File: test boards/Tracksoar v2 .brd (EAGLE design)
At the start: 50.4 x 19.6 mm, 48 parts, among them IC1 BME280, IC2 74AHC1G125DBV, Y1 16MHZ

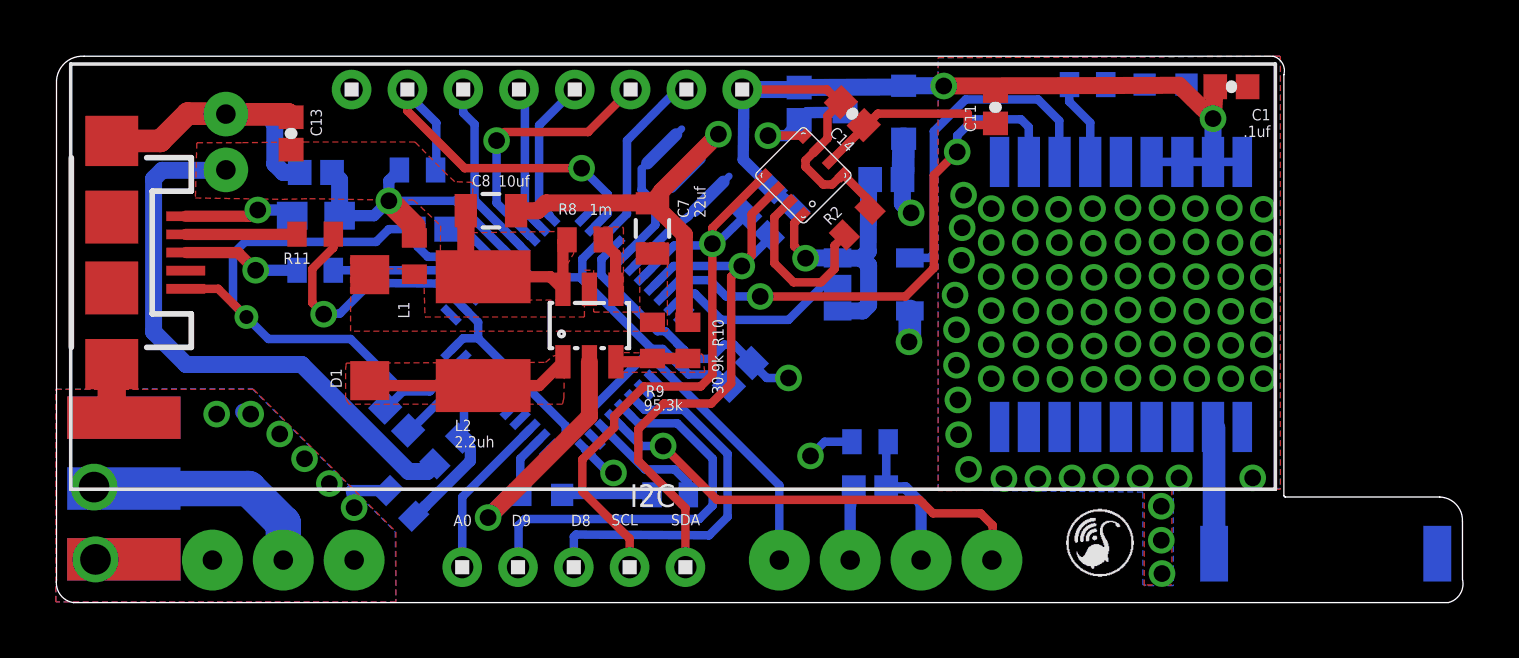
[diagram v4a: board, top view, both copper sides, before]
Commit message: Silkscreen cleanup and additional analog pin
removed as many silkscreen keep out errors as possible. Added a
breakout for analog pin A1 to the bottom header.
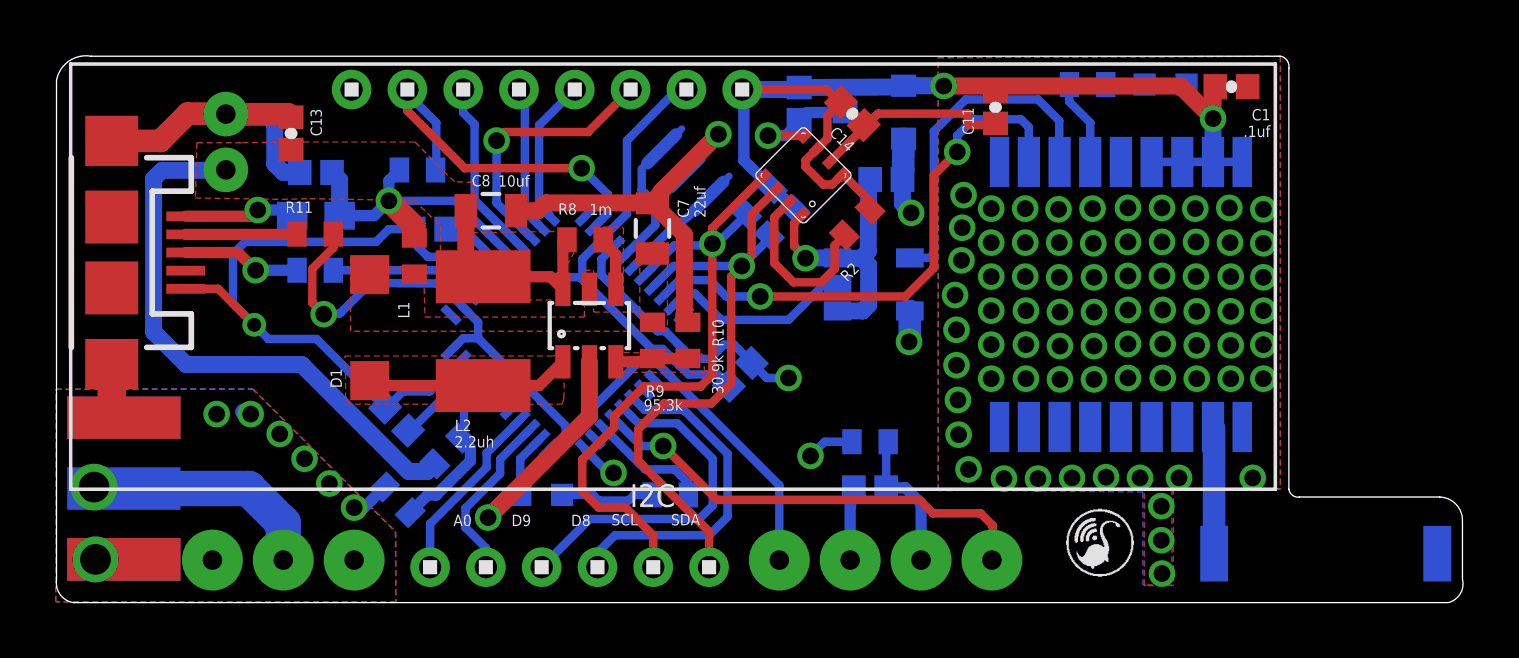
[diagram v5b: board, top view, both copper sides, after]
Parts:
- U$3: value 1X5 -> 1X6; device headers(2mm):1X5 -> headers(2mm):1X6
- moved C6 0.18 mm to (12.2, 3.66)
- moved U$3 0.15 mm to (18.4, 1.24)
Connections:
- new net A1: U$3.1, U$4.37
- net A0: now also U$3.2; no longer U$3.1
- net D8: now also U$3.4; no longer U$3.3
- net D9: now also U$3.3; no longer U$3.2
- net SCL: now also U$3.5; no longer U$3.4
- net SDA: now also U$3.6; no longer U$3.5
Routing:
- net A1: track 0.00 -> 6.63 mm
- net D9: track 14.3 -> 12.6 mm
- net D8: track 13.3 -> 12.1 mm
- net SCL: track 23.2 -> 24.1 mm
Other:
- outline, holes or cut-outs redrawn

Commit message: Moved BME280
moved the bme 280 sensor away from the 3v regulator to help mitigate thermal issues.
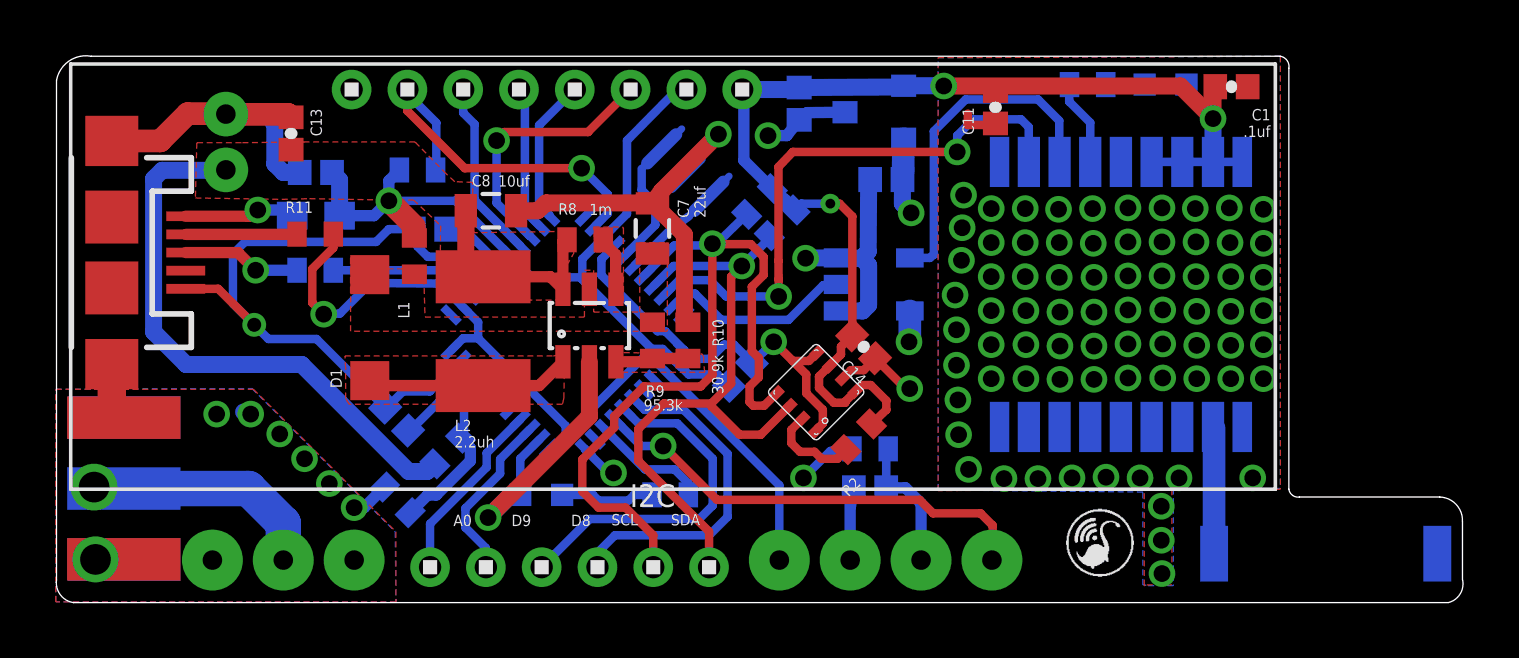
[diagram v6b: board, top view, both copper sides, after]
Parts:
- moved C14 8.37 mm to (29.0, 9.14)
- moved IC1 7.79 mm to (27.3, 7.52)
- moved R2 7.70 mm to (28.8, 5.92)
- moved R12 0.25 mm to (29.2, 5.49)
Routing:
- net SCL: track 24.1 -> 29.8 mm
- net N$2: track 6.69 -> 3.37 mm
- net 3V: track 40.5 -> 43.7 mm, vias 2 -> 3
- net RX: track 19.8 -> 20.6 mm
- net GND: track 104.0 -> 104.6 mm, vias 86 -> 87
- net SDA: track 22.6 -> 23.1 mm

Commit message: Removed Pours
removed pours from under the lm3480 to limit heat reaching the bme280
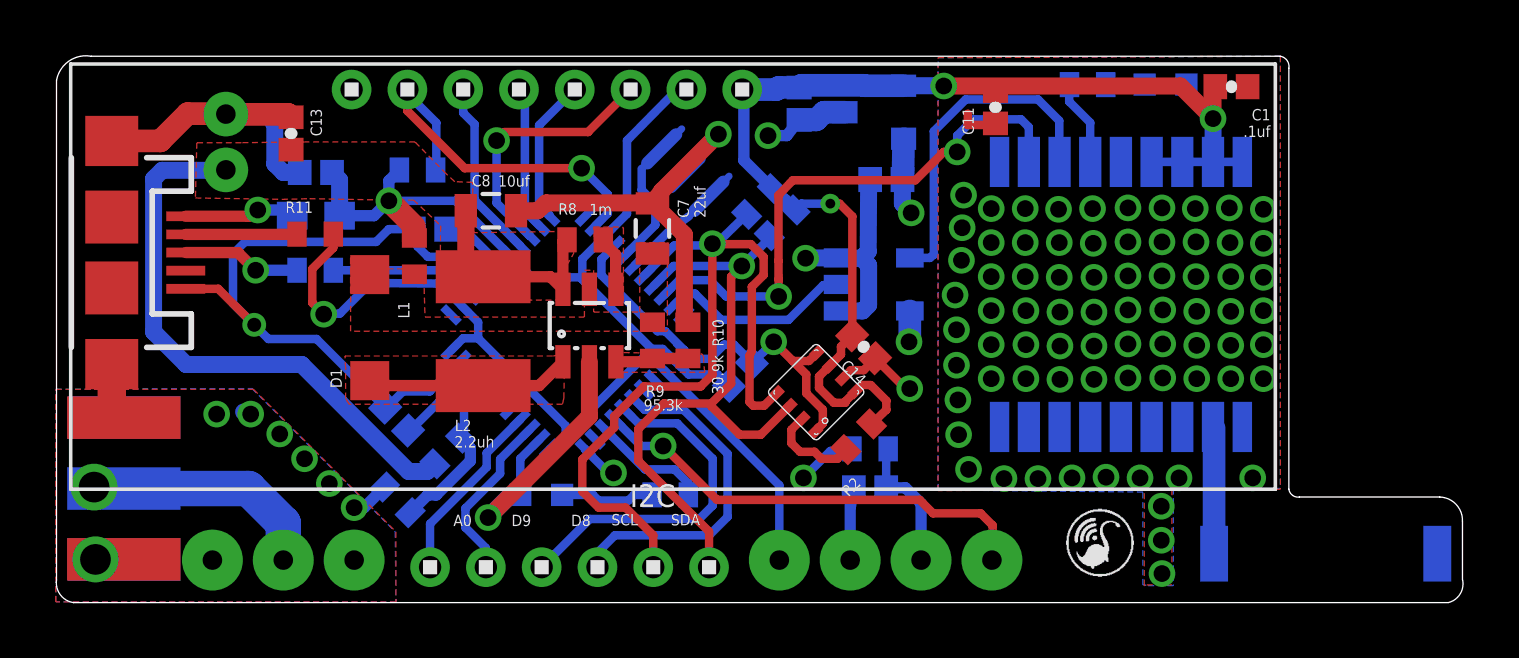
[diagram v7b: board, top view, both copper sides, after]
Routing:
- net GND: track 104.6 -> 101.8 mm
- net RX: track 20.6 -> 20.0 mm
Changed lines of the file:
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@@
 <layers>
 <layer number="1" name="Top" color="4" fill="1" visible="yes" active="yes"/>
-<layer number="2" name="Route2" color="6" fill="1" visible="no" active="yes"/>
+<layer number="2" name="Route2" color="6" fill="1" visible="yes" active="yes"/>
 <layer number="3" name="Route3" color="4" fill="3" visible="no" active="no"/>
 <layer number="14" name="Route14" color="1" fill="6" visible="no" active="no"/>
-<layer number="15" name="Route15" color="3" fill="1" visible="no" active="yes"/>
+<layer number="15" name="Route15" color="3" fill="1" visible="yes" active="yes"/>
 <layer number="16" name="Bottom" color="1" fill="1" visible="yes" active="yes"/>
 <layer number="17" name="Pads" color="2" fill="1" visible="yes" active="yes"/>
@@
 <polygon width="0.4064" layer="2">
 <vertex x="0" y="19.5326"/>
+<vertex x="26.3652" y="19.5834"/>
+<vertex x="26.416" y="15.0876"/>
+<vertex x="32.3088" y="15.0876"/>
+<vertex x="32.3342" y="19.5326"/>
 <vertex x="43.8658" y="19.5326"/>
 <vertex x="43.8658" y="4.0386"/>
@@
 <wire x1="25.527" y1="16.7132" x2="26.2024" y2="16.7132" width="0.4064" layer="16"/>
 <wire x1="26.2024" y1="16.7132" x2="26.6446" y2="17.2762" width="0.4064" layer="16"/>
-<wire x1="26.6446" y1="17.2762" x2="26.9266" y2="17.5364" width="0.4064" layer="16"/>
-<wire x1="26.9266" y1="17.5364" x2="28.2878" y2="17.5514" width="0.4064" layer="16"/>
 <wire x1="29.7646" y1="4.0894" x2="30.4546" y2="4.0894" width="0.4064" layer="16"/>
 <wire x1="30.4546" y1="4.0894" x2="31.0134" y2="3.5306" width="0.4064" layer="16"/>
@@
 <wire x1="26.8834" y1="12.3292" x2="26.8732" y2="12.319" width="0.6096" layer="16"/>
 <via x="26.8732" y="12.319" extent="1-16" drill="0.6"/>
-<wire x1="26.8732" y1="12.319" x2="26.4668" y2="12.319" width="0.6096" layer="2"/>
-<wire x1="26.4668" y1="12.319" x2="26.3144" y2="12.1666" width="0.6096" layer="2"/>
 <wire x1="28.0216" y1="10.4292" x2="28.9204" y2="10.4292" width="0.6096" layer="16"/>
 <wire x1="28.9204" y1="10.4292" x2="29.1338" y2="10.6426" width="0.6096" layer="16"/>
@@
 <wire x1="25.432846875" y1="9.017" x2="25.7302" y2="9.3218" width="0.3048" layer="16"/>
 <via x="25.7302" y="9.3218" extent="1-16" drill="0.6"/>
-<wire x1="25.7302" y1="9.3218" x2="26.3652" y2="8.128" width="0.3048" layer="2"/>
-<wire x1="26.3652" y1="8.128" x2="27.1526" y2="8.128" width="0.3048" layer="2"/>
 <wire x1="12.446" y1="7.5438" x2="11.865521875" y2="6.963321875" width="0.3048" layer="16"/>
 <wire x1="11.865521875" y1="6.963321875" x2="11.807278125" y2="6.963321875" width="0.3048" layer="16"/>
@@
 <wire x1="29.366121875" y1="8.733875" x2="30.454596875" y2="7.6454" width="0.3048" layer="1"/>
 <wire x1="30.454596875" y1="7.6454" x2="30.607" y2="7.6454" width="0.3048" layer="1"/>
+<wire x1="26.6446" y1="17.2762" x2="27.2584" y2="17.2762" width="0.8128" layer="16"/>
+<wire x1="27.2584" y1="17.2762" x2="27.5336" y2="17.5514" width="0.8128" layer="16"/>
+<wire x1="27.5336" y1="17.5514" x2="28.2878" y2="17.5514" width="0.8128" layer="16"/>
 </signal>
 <signal name="VCC">
@@
 <polygon width="0.4064" layer="15">
 <vertex x="0" y="19.5326"/>
+<vertex x="26.3906" y="19.5834"/>
+<vertex x="26.416" y="15.0876"/>
+<vertex x="32.3342" y="15.0876"/>
+<vertex x="32.3596" y="19.5326"/>
 <vertex x="43.942" y="19.5326"/>
 <vertex x="43.942" y="4.0132"/>
@@
 <wire x1="30.6116" y1="9.3518" x2="30.5816" y2="9.3218" width="0.8128" layer="16"/>
 <via x="30.5816" y="9.3218" extent="1-16" drill="0.6"/>
-<wire x1="30.5816" y1="9.3218" x2="30.5816" y2="8.3058" width="0.8128" layer="15"/>
-<wire x1="30.5816" y1="8.3058" x2="30.607" y2="8.2804" width="0.8128" layer="15"/>
+<wire x1="30.5816" y1="9.3218" x2="30.5562" y2="8.9916" width="0.8128" layer="15"/>
+<wire x1="30.5562" y1="8.9916" x2="30.6324" y2="9.2456" width="0.8128" layer="15"/>
 <wire x1="30.368" y1="15.402" x2="30.3488" y2="15.1384" width="0.6096" layer="16"/>
 <wire x1="30.3488" y1="15.1384" x2="30.3426" y2="14.2852" width="0.6096" layer="16"/>
@@
 <wire x1="40.377" y1="15.7704" x2="39.277" y2="15.7704" width="0.3048" layer="16"/>
 <contactref element="FTDI" pad="1"/>
-<wire x1="24.6022" y1="18.3642" x2="26.2994" y2="18.3642" width="0.6096" layer="16"/>
-<wire x1="26.2994" y1="18.3642" x2="26.6446" y2="18.4362" width="0.4064" layer="16"/>
-<wire x1="26.6446" y1="18.4362" x2="30.3418" y2="18.4554" width="0.6096" layer="16"/>
-<wire x1="30.3418" y1="18.4554" x2="30.3878" y2="18.5014" width="0.4064" layer="16"/>
 <wire x1="41.5586" y1="18.4658" x2="41.4782" y2="18.4658" width="0.6096" layer="1"/>
 <wire x1="41.4782" y1="18.4658" x2="41.4782" y2="17.3332" width="0.6096" layer="1"/>
@@
 <wire x1="28.5496" y1="9.557846875" x2="28.545875" y2="9.554121875" width="0.3048" layer="1"/>
 <wire x1="26.720803125" y1="14.2748" x2="27.7622" y2="14.2748" width="0.3048" layer="16"/>
+<wire x1="28.9780625" y1="18.5014" x2="30.3878" y2="18.5014" width="0.8128" layer="16"/>
+<wire x1="26.6446" y1="18.4362" x2="26.725" y2="18.5166" width="0.8128" layer="16"/>
+<wire x1="26.725" y1="18.5166" x2="28.9628625" y2="18.5166" width="0.8128" layer="16"/>
+<wire x1="28.9628625" y1="18.5166" x2="28.9780625" y2="18.5014" width="0.8128" layer="16"/>
+<wire x1="24.6022" y1="18.3642" x2="25.8318" y2="18.3642" width="0.8128" layer="16"/>
+<wire x1="25.8318" y1="18.3642" x2="25.908" y2="18.4404" width="0.8128" layer="16"/>
+<wire x1="25.908" y1="18.4404" x2="26.6404" y2="18.4404" width="0.8128" layer="16"/>
+<wire x1="26.6404" y1="18.4404" x2="26.6446" y2="18.4362" width="0.8128" layer="16"/>
 </signal>
 <signal name="N$1">
@@
 <wire x1="20.4216" y1="3.3782" x2="21.415" y2="2.3848" width="0.3048" layer="1"/>
 <wire x1="21.415" y1="2.3848" x2="21.415" y2="1.2446" width="0.3048" layer="1"/>
-<wire x1="24.9476" y1="8.99763125" x2="25.1968" y2="8.74843125" width="0.3048" layer="1"/>
+<wire x1="24.9476" y1="8.99763125" x2="24.8666" y2="8.82463125" width="0.3048" layer="1"/>
 <wire x1="25.3698" y1="11.71543125" x2="25.3698" y2="12.36376875" width="0.3048" layer="1"/>
 <wire x1="25.3698" y1="12.36376875" x2="24.91136875" y2="12.8222" width="0.3048" layer="1"/>
@@
 <wire x1="24.9476" y1="8.99763125" x2="24.9476" y2="11.29323125" width="0.3048" layer="1"/>
 <wire x1="24.9476" y1="11.29323125" x2="25.3698" y2="11.71543125" width="0.3048" layer="1"/>
-<wire x1="25.1968" y1="8.74843125" x2="25.1968" y2="8.0518" width="0.3048" layer="1"/>
-<wire x1="24.8666" y1="7.7216" x2="24.8666" y2="7.1628" width="0.3048" layer="1"/>
+<wire x1="24.8666" y1="8.82463125" x2="24.8666" y2="7.1628" width="0.3048" layer="1"/>
 <wire x1="24.8666" y1="7.1628" x2="24.9936" y2="7.0358" width="0.3048" layer="1"/>
 <wire x1="25.392740625" y1="7.0358" x2="25.839984375" y2="7.48304375" width="0.3048" layer="1"/>
-<wire x1="25.1968" y1="8.0518" x2="24.8666" y2="7.7216" width="0.3048" layer="1"/>
 <wire x1="24.9936" y1="7.0358" x2="25.392740625" y2="7.0358" width="0.3048" layer="1"/>
 </signal>
@@
 <wire x1="25.908" y1="10.9474" x2="25.908" y2="11.56783125" width="0.3048" layer="1"/>
 <wire x1="25.908" y1="11.56783125" x2="25.9032" y2="12.22343125" width="0.3048" layer="1"/>
-<wire x1="25.9032" y1="15.5908" x2="26.416" y2="16.129" width="0.3048" layer="1"/>
-<wire x1="25.9032" y1="12.22343125" x2="25.9032" y2="15.5908" width="0.3048" layer="1"/>
-<wire x1="26.416" y1="16.129" x2="32.3088" y2="16.129" width="0.3048" layer="1"/>
+<wire x1="25.9032" y1="14.5748" x2="26.416" y2="15.113" width="0.3048" layer="1"/>
+<wire x1="25.9032" y1="12.22343125" x2="25.9032" y2="14.5748" width="0.3048" layer="1"/>
+<wire x1="26.416" y1="15.113" x2="30.8102" y2="15.113" width="0.3048" layer="1"/>
+<wire x1="30.8102" y1="15.113" x2="31.8262" y2="16.129" width="0.3048" layer="1"/>
+<wire x1="31.8262" y1="16.129" x2="32.3088" y2="16.129" width="0.3048" layer="1"/>
 </signal>
 <signal name="N$20">
@@
 <wire x1="19.9898" y1="4.6228" x2="20.7518" y2="4.6228" width="0.3048" layer="15"/>
 <wire x1="20.7518" y1="4.6228" x2="21.2852" y2="4.0894" width="0.3048" layer="15"/>
-<wire x1="21.2852" y1="4.0894" x2="25.908" y2="4.0894" width="0.3048" layer="15"/>
-<wire x1="25.908" y1="4.0894" x2="26.797" y2="4.445" width="0.3048" layer="15"/>
+<wire x1="21.2852" y1="4.0894" x2="26.4414" y2="4.0894" width="0.3048" layer="15"/>
+<wire x1="26.4414" y1="4.0894" x2="26.797" y2="4.445" width="0.3048" layer="15"/>
 <via x="26.797" y="4.445" extent="1-16" drill="0.6"/>
 <wire x1="26.797" y1="4.445" x2="27.7622" y2="5.4102" width="0.3048" layer="16"/>
